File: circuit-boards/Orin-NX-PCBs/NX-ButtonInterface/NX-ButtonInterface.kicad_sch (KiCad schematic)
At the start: 3 parts, among them J1 NX CONTROL & UART, J2 CAN-NX, J3 NX-BUTTON

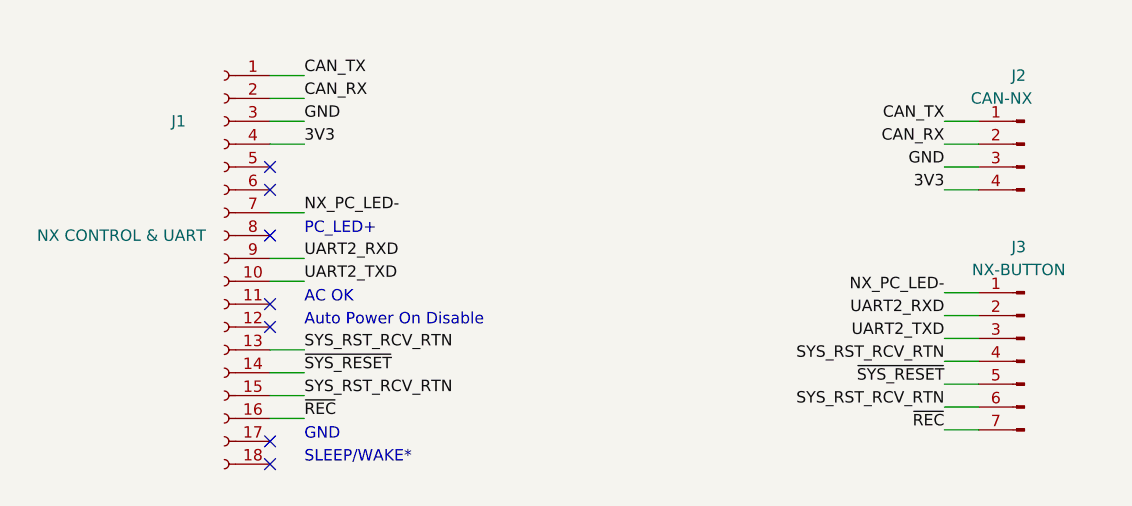
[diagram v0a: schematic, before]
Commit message: Change SL connectors to surface mount solder wires.
Signed-off-by: Scott Berman <sgberman1@gmail.com>
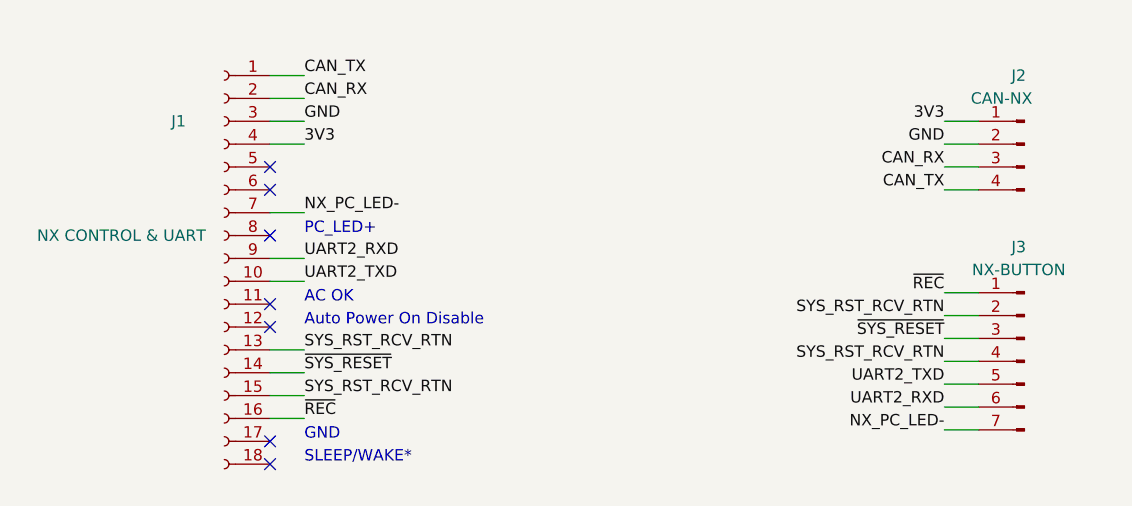
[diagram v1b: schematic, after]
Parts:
- J2: footprint NX-ButtonInterface:70543-0003 -> NX-ButtonInterface:4-pin-solder-pads; DIST Digikey -> (none); DIST P/N WM4802-ND -> (none); MFG Molex -> (none); MFG P/N 0705430003 -> (none)
- J3: footprint NX-ButtonInterface:70543-0006 -> NX-ButtonInterface:7-pin-solder-pads; DIST Digikey -> (none); DIST P/N WM4805-ND -> (none); MFG Molex -> (none); MFG P/N 0705430006 -> (none)
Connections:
- net 3V3: now also J2.1 (Pin_1); no longer J2.4 (Pin_4)
- net CAN_RX: now also J2.3 (Pin_3); no longer J2.2 (Pin_2)
- net CAN_TX: now also J2.4 (Pin_4); no longer J2.1 (Pin_1)
- net GND: now also J2.2 (Pin_2); no longer J2.3 (Pin_3)
- net NX_PC_LED-: now also J3.7 (Pin_7); no longer J3.1 (Pin_1)
- net SYS_RST_RCV_RTN: now also J3.2 (Pin_2); no longer J3.6 (Pin_6)
- net UART2_RXD: now also J3.6 (Pin_6); no longer J3.2 (Pin_2)
- net UART2_TXD: now also J3.5 (Pin_5); no longer J3.3 (Pin_3)
- net ~{REC}: now also J3.1 (Pin_1); no longer J3.7 (Pin_7)
- net ~{SYS_RESET}: now also J3.3 (Pin_3); no longer J3.5 (Pin_5)
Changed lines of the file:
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@@
     (effects (font (size 1.27 1.27)) (justify left bottom))
+  )
+  (label "UART2_TXD" (at 166.37 106.68 180) (fields_autoplaced)
+    (effects (font (size 1.27 1.27)) (justify right bottom))
   )
   (label "~{SYS_RESET}" (at 95.25 105.41 0) (fields_autoplaced)
     (effects (font (size 1.27 1.27)) (justify left bottom))
   )
-  (label "UART2_TXD" (at 166.37 101.6 180) (fields_autoplaced)
-    (effects (font (size 1.27 1.27)) (justify right bottom))
-  )
   (label "CAN_TX" (at 95.25 72.39 0) (fields_autoplaced)
     (effects (font (size 1.27 1.27)) (justify left bottom))
   )
-  (label "3V3" (at 166.37 85.09 180) (fields_autoplaced)
+  (label "~{SYS_RESET}" (at 166.37 101.6 180) (fields_autoplaced)
     (effects (font (size 1.27 1.27)) (justify right bottom))
   )
@@
     (effects (font (size 1.27 1.27)) (justify left bottom))
   )
+  (label "UART2_RXD" (at 166.37 109.22 180) (fields_autoplaced)
+    (effects (font (size 1.27 1.27)) (justify right bottom))
+  )
   (label "~{REC}" (at 95.25 110.49 0) (fields_autoplaced)
     (effects (font (size 1.27 1.27)) (justify left bottom))
   )
-  (label "UART2_RXD" (at 166.37 99.06 180) (fields_autoplaced)
+  (label "3V3" (at 166.37 77.47 180) (fields_autoplaced)
     (effects (font (size 1.27 1.27)) (justify right bottom))
   )
-  (label "~{REC}" (at 166.37 111.76 180) (fields_autoplaced)
+  (label "CAN_TX" (at 166.37 85.09 180) (fields_autoplaced)
+    (effects (font (size 1.27 1.27)) (justify right bottom))
+  )
+  (label "~{REC}" (at 166.37 96.52 180) (fields_autoplaced)
     (effects (font (size 1.27 1.27)) (justify right bottom))
   )
@@
     (effects (font (size 1.27 1.27)) (justify left bottom))
   )
-  (label "CAN_TX" (at 166.37 77.47 180) (fields_autoplaced)
+  (label "NX_PC_LED-" (at 166.37 111.76 180) (fields_autoplaced)
     (effects (font (size 1.27 1.27)) (justify right bottom))
   )
-  (label "~{SYS_RESET}" (at 166.37 106.68 180) (fields_autoplaced)
+  (label "SYS_RST_RCV_RTN" (at 166.37 104.14 180) (fields_autoplaced)
     (effects (font (size 1.27 1.27)) (justify right bottom))
   )
-  (label "NX_PC_LED-" (at 166.37 96.52 180) (fields_autoplaced)
+  (label "GND" (at 166.37 80.01 180) (fields_autoplaced)
     (effects (font (size 1.27 1.27)) (justify right bottom))
   )
-  (label "CAN_RX" (at 166.37 80.01 180) (fields_autoplaced)
+  (label "SYS_RST_RCV_RTN" (at 166.37 99.06 180) (fields_autoplaced)
     (effects (font (size 1.27 1.27)) (justify right bottom))
   )
@@
     (effects (font (size 1.27 1.27)) (justify left bottom))
   )
-  (label "GND" (at 166.37 82.55 180) (fields_autoplaced)
-    (effects (font (size 1.27 1.27)) (justify right bottom))
-  )
   (label "UART2_RXD" (at 95.25 92.71 0) (fields_autoplaced)
     (effects (font (size 1.27 1.27)) (justify left bottom))
   )
-  (label "SYS_RST_RCV_RTN" (at 166.37 109.22 180) (fields_autoplaced)
+  (label "CAN_RX" (at 166.37 82.55 180) (fields_autoplaced)
     (effects (font (size 1.27 1.27)) (justify right bottom))
   )
@@
   (label "NX_PC_LED-" (at 95.25 87.63 0) (fields_autoplaced)
     (effects (font (size 1.27 1.27)) (justify left bottom))
-  )
-  (label "SYS_RST_RCV_RTN" (at 166.37 104.14 180) (fields_autoplaced)
-    (effects (font (size 1.27 1.27)) (justify right bottom))
   )
   (label "SYS_RST_RCV_RTN" (at 95.25 102.87 0) (fields_autoplaced)
@@
       (effects (font (size 1.27 1.27)))
     )
-    (property "Footprint" "NX-ButtonInterface:70543-0003" (at 175.26 80.01 0)
+    (property "Footprint" "NX-ButtonInterface:4-pin-solder-pads" (at 175.26 80.01 0)
       (effects (font (size 1.27 1.27)) hide)
     )
-    (property "Datasheet" "Components/Molex-70543-0001.pdf" (at 175.26 80.01 0)
+    (property "Datasheet" "" (at 175.26 80.01 0)
       (effects (font (size 1.27 1.27)) hide)
     )
-    (property "MFG" "Molex" (at 175.26 80.01 0)
+    (property "MFG" "" (at 175.26 80.01 0)
       (effects (font (size 1.27 1.27)) hide)
     )
-    (property "MFG P/N" "0705430003" (at 175.26 80.01 0)
+    (property "MFG P/N" "" (at 175.26 80.01 0)
       (effects (font (size 1.27 1.27)) hide)
     )
-    (property "DIST" "Digikey" (at 175.26 80.01 0)
+    (property "DIST" "" (at 175.26 80.01 0)
       (effects (font (size 1.27 1.27)) hide)
     )
-    (property "DIST P/N" "WM4802-ND" (at 175.26 80.01 0)
+    (property "DIST P/N" "" (at 175.26 80.01 0)
       (effects (font (size 1.27 1.27)) hide)
     )
@@
       (effects (font (size 1.27 1.27)))
     )
-    (property "Footprint" "NX-ButtonInterface:70543-0006" (at 175.26 104.14 0)
+    (property "Footprint" "NX-ButtonInterface:7-pin-solder-pads" (at 175.26 104.14 0)
       (effects (font (size 1.27 1.27)) hide)
     )
-    (property "Datasheet" "Components/Molex-70543-0001.pdf" (at 175.26 104.14 0)
+    (property "Datasheet" "" (at 175.26 104.14 0)
       (effects (font (size 1.27 1.27)) hide)
     )
-    (property "DIST" "Digikey" (at 175.26 104.14 0)
+    (property "DIST" "" (at 175.26 104.14 0)
       (effects (font (size 1.27 1.27)) hide)
     )
-    (property "DIST P/N" "WM4805-ND" (at 175.26 104.14 0)
+    (property "DIST P/N" "" (at 175.26 104.14 0)
       (effects (font (size 1.27 1.27)) hide)
     )
-    (property "MFG" "Molex" (at 175.26 104.14 0)
+    (property "MFG" "" (at 175.26 104.14 0)
       (effects (font (size 1.27 1.27)) hide)
     )
-    (property "MFG P/N" "0705430006" (at 175.26 104.14 0)
+    (property "MFG P/N" "" (at 175.26 104.14 0)
       (effects (font (size 1.27 1.27)) hide)
     )

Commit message: Intermediate checkin of NX-Indicator-board
Signed-off-by: Scott Berman <scott.berman@bluerivertech.com>
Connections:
- net 3V3: now also J2.4 (Pin_4); no longer J2.1 (Pin_1)
- net CAN_RX: now also J2.2 (Pin_2); no longer J2.3 (Pin_3)
- net CAN_TX: now also J2.1 (Pin_1); no longer J2.4 (Pin_4)
- net GND: now also J2.3 (Pin_3); no longer J2.2 (Pin_2)
- net NX_PC_LED-: now also J3.1 (Pin_1); no longer J3.7 (Pin_7)
- net SYS_RST_RCV_RTN: now also J3.6 (Pin_6); no longer J3.2 (Pin_2)
- net UART2_RXD: now also J3.2 (Pin_2); no longer J3.6 (Pin_6)
- net UART2_TXD: now also J3.3 (Pin_3); no longer J3.5 (Pin_5)
- net ~{REC}: now also J3.7 (Pin_7); no longer J3.1 (Pin_1)
- net ~{SYS_RESET}: now also J3.5 (Pin_5); no longer J3.3 (Pin_3)
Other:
- note added: "7" wires"
- note added: "BLACK"
- note added: "BLUE"
- note added: "GREEN"
- note added: "RED"
- note added: "WHITE"
- note added: "YELLOW"
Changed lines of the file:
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@@
     (stroke (width 0) (type default))
   )
+  (text "RED" (at 85.09 80.01 0)
+    (effects (font (size 1.27 1.27)) (justify right bottom))
+  )
+  (text "YELLOW" (at 85.09 74.93 0)
+    (effects (font (size 1.27 1.27)) (justify right bottom))
+  )
+  (text "GREEN" (at 85.09 72.39 0)
+    (effects (font (size 1.27 1.27)) (justify right bottom))
+  )
+  (text "GREEN" (at 176.53 86.36 0)
+    (effects (font (size 1.27 1.27)) (justify left bottom))
+  )
+  (text "BLACK" (at 86.36 87.63 0)
+    (effects (font (size 1.27 1.27)) (justify right bottom))
+  )
+  (text "GREEN" (at 85.09 110.49 0)
+    (effects (font (size 1.27 1.27)) (justify right bottom))
+  )
+  (text "RED" (at 176.53 78.74 0)
+    (effects (font (size 1.27 1.27)) (justify left bottom))
+  )
+  (text "WHITE" (at 85.09 92.71 0)
+    (effects (font (size 1.27 1.27)) (justify right bottom))
+  )
+  (text "BLACK" (at 85.09 77.47 0)
+    (effects (font (size 1.27 1.27)) (justify right bottom))
+  )
+  (text "BLUE" (at 85.09 107.95 0)
+    (effects (font (size 1.27 1.27)) (justify right bottom))
+  )
+  (text "YELLOW" (at 176.53 102.87 0)
+    (effects (font (size 1.27 1.27)) (justify left bottom))
+  )
+  (text "7\" wires" (at 128.27 73.66 0)
+    (effects (font (size 1.27 1.27)) (justify left bottom))
+  )
   (text "AC OK" (at 95.25 97.79 0)
     (effects (font (size 1.27 1.27)) (justify left bottom))
   )
+  (text "RED" (at 85.09 95.25 0)
+    (effects (font (size 1.27 1.27)) (justify right bottom))
+  )
+  (text "GREEN" (at 176.53 97.79 0)
+    (effects (font (size 1.27 1.27)) (justify left bottom))
+  )
+  (text "BLUE" (at 85.09 102.87 0)
+    (effects (font (size 1.27 1.27)) (justify right bottom))
+  )
+  (text "YELLOW" (at 85.09 105.41 0)
+    (effects (font (size 1.27 1.27)) (justify right bottom))
+  )
   (text "GND" (at 95.25 113.03 0)
     (effects (font (size 1.27 1.27)) (justify left bottom))
@@
     (effects (font (size 1.27 1.27)) (justify left bottom))
   )
+  (text "BLUE" (at 176.53 100.33 0)
+    (effects (font (size 1.27 1.27)) (justify left bottom))
+  )
+  (text "BLACK" (at 176.53 113.03 0)
+    (effects (font (size 1.27 1.27)) (justify left bottom))
+  )
+  (text "YELLOW" (at 176.53 83.82 0)
+    (effects (font (size 1.27 1.27)) (justify left bottom))
+  )
+  (text "BLACK" (at 176.53 81.28 0)
+    (effects (font (size 1.27 1.27)) (justify left bottom))
+  )
+  (text "RED" (at 176.53 107.95 0)
+    (effects (font (size 1.27 1.27)) (justify left bottom))
+  )
   (text "Auto Power On Disable" (at 95.25 100.33 0)
     (effects (font (size 1.27 1.27)) (justify left bottom))
   )
+  (text "BLUE" (at 176.53 105.41 0)
+    (effects (font (size 1.27 1.27)) (justify left bottom))
+  )
+  (text "WHITE" (at 176.53 110.49 0)
+    (effects (font (size 1.27 1.27)) (justify left bottom))
+  )
   (text "SLEEP/WAKE*" (at 95.25 115.57 0)
     (effects (font (size 1.27 1.27)) (justify left bottom))
@@
     (effects (font (size 1.27 1.27)) (justify left bottom))
   )
-  (symbol (lib_id "Connector:Conn_01x04_Pin") (at 175.26 80.01 0) (mirror y) (unit 1)
+  (symbol (lib_id "Connector:Conn_01x07_Pin") (at 175.26 104.14 180) (unit 1)
     (in_bom yes) (on_board yes) (dnp no)
-    (property "Reference" "J2" (at 174.625 72.39 0)
-      (effects (font (size 1.27 1.27)))
-    )
-    (property "Value" "CAN-NX" (at 172.72 74.93 0)
-      (effects (font (size 1.27 1.27)))
-    )
-    (property "Footprint" "NX-ButtonInterface:4-pin-solder-pads" (at 175.26 80.01 0)
-      (effects (font (size 1.27 1.27)) hide)
-    )
-    (property "Datasheet" "" (at 175.26 80.01 0)
-      (effects (font (size 1.27 1.27)) hide)
-    )
-    (property "MFG" "" (at 175.26 80.01 0)
-      (effects (font (size 1.27 1.27)) hide)
-    )
-    (property "MFG P/N" "" (at 175.26 80.01 0)
-      (effects (font (size 1.27 1.27)) hide)
-    )
-    (property "DIST" "" (at 175.26 80.01 0)
-      (effects (font (size 1.27 1.27)) hide)
-    )
-    (property "DIST P/N" "" (at 175.26 80.01 0)
-      (effects (font (size 1.27 1.27)) hide)
-    )
-    (pin "1")
-    (pin "2")
-    (pin "3")
-    (pin "4")
-    (instances
-      (project "NX-ButtonInterface"
-        (path "/a7eb5823-c87f-41de-b6ed-af0ad18b6b3c"
-          (reference "J2") (unit 1)
-        )
-      )
-    )
-  )
-  (symbol (lib_id "Connector:Conn_01x07_Pin") (at 175.26 104.14 0) (mirror y) (unit 1)
-    (in_bom yes) (on_board yes) (dnp no)
-    (property "Reference" "J3" (at 174.625 91.44 0)
-      (effects (font (size 1.27 1.27)))
-    )
-    (property "Value" "NX-BUTTON" (at 174.625 93.98 0)
+    (property "Reference" "J3" (at 174.625 116.84 0)
+      (effects (font (size 1.27 1.27)))
+    )
+    (property "Value" "NX-BUTTON" (at 174.625 114.3 0)
       (effects (font (size 1.27 1.27)))
     )
@@
   (symbol (lib_id "Connector:Conn_01x18_Socket") (at 86.36 92.71 0) (mirror y) (unit 1)
     (in_bom yes) (on_board yes) (dnp no)
-    (property "Reference" "J1" (at 81.28 77.47 0)
-      (effects (font (size 1.27 1.27)))
-    )
-    (property "Value" "NX CONTROL & UART" (at 74.93 90.17 0)
+    (property "Reference" "J1" (at 87.63 69.85 0)
+      (effects (font (size 1.27 1.27)))
+    )
+    (property "Value" "NX CONTROL & UART" (at 88.9 67.31 0)
       (effects (font (size 1.27 1.27)))
     )
@@
         )
       )
+    )
+  )
+  (symbol (lib_id "Connector:Conn_01x04_Pin") (at 175.26 82.55 180) (unit 1)
+    (in_bom yes) (on_board yes) (dnp no)
+    (property "Reference" "J2" (at 174.625 90.17 0)
+      (effects (font (size 1.27 1.27)))
+    )
+    (property "Value" "CAN-NX" (at 172.72 87.63 0)
+      (effects (font (size 1.27 1.27)))
+    )
+    (property "Footprint" "NX-ButtonInterface:4-pin-solder-pads" (at 175.26 82.55 0)
+      (effects (font (size 1.27 1.27)) hide)
+    )
+    (property "Datasheet" "" (at 175.26 82.55 0)
+      (effects (font (size 1.27 1.27)) hide)
+    )
+    (property "MFG" "" (at 175.26 82.55 0)
+      (effects (font (size 1.27 1.27)) hide)
+    )
+    (property "MFG P/N" "" (at 175.26 82.55 0)
+      (effects (font (size 1.27 1.27)) hide)
+    )
+    (property "DIST" "" (at 175.26 82.55 0)
+      (effects (font (size 1.27 1.27)) hide)
+    )
+    (property "DIST P/N" "" (at 175.26 82.55 0)
+      (effects (font (size 1.27 1.27)) hide)
+    )
+    (pin "1")
+    (pin "2")
+    (pin "3")
+    (pin "4")
+    (instances
+      (project "NX-ButtonInterface"
+        (path "/a7eb5823-c87f-41de-b6ed-af0ad18b6b3c"
+          (reference "J2") (unit 1)
+        )
+      )
